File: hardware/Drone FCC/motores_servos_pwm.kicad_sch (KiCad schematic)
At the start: 13 parts, among them J301 ESC 1, J302 ESC 2, J303 ESC 3, J304 ESC 4, J305 ESC 5, J306 ESC 6, J307 ESC 7, J308 ESC 8, J309 SERVO 1, J310 SERVO 2, J311 SERVO 3, J312 SERVO 4, J313 Power Servo

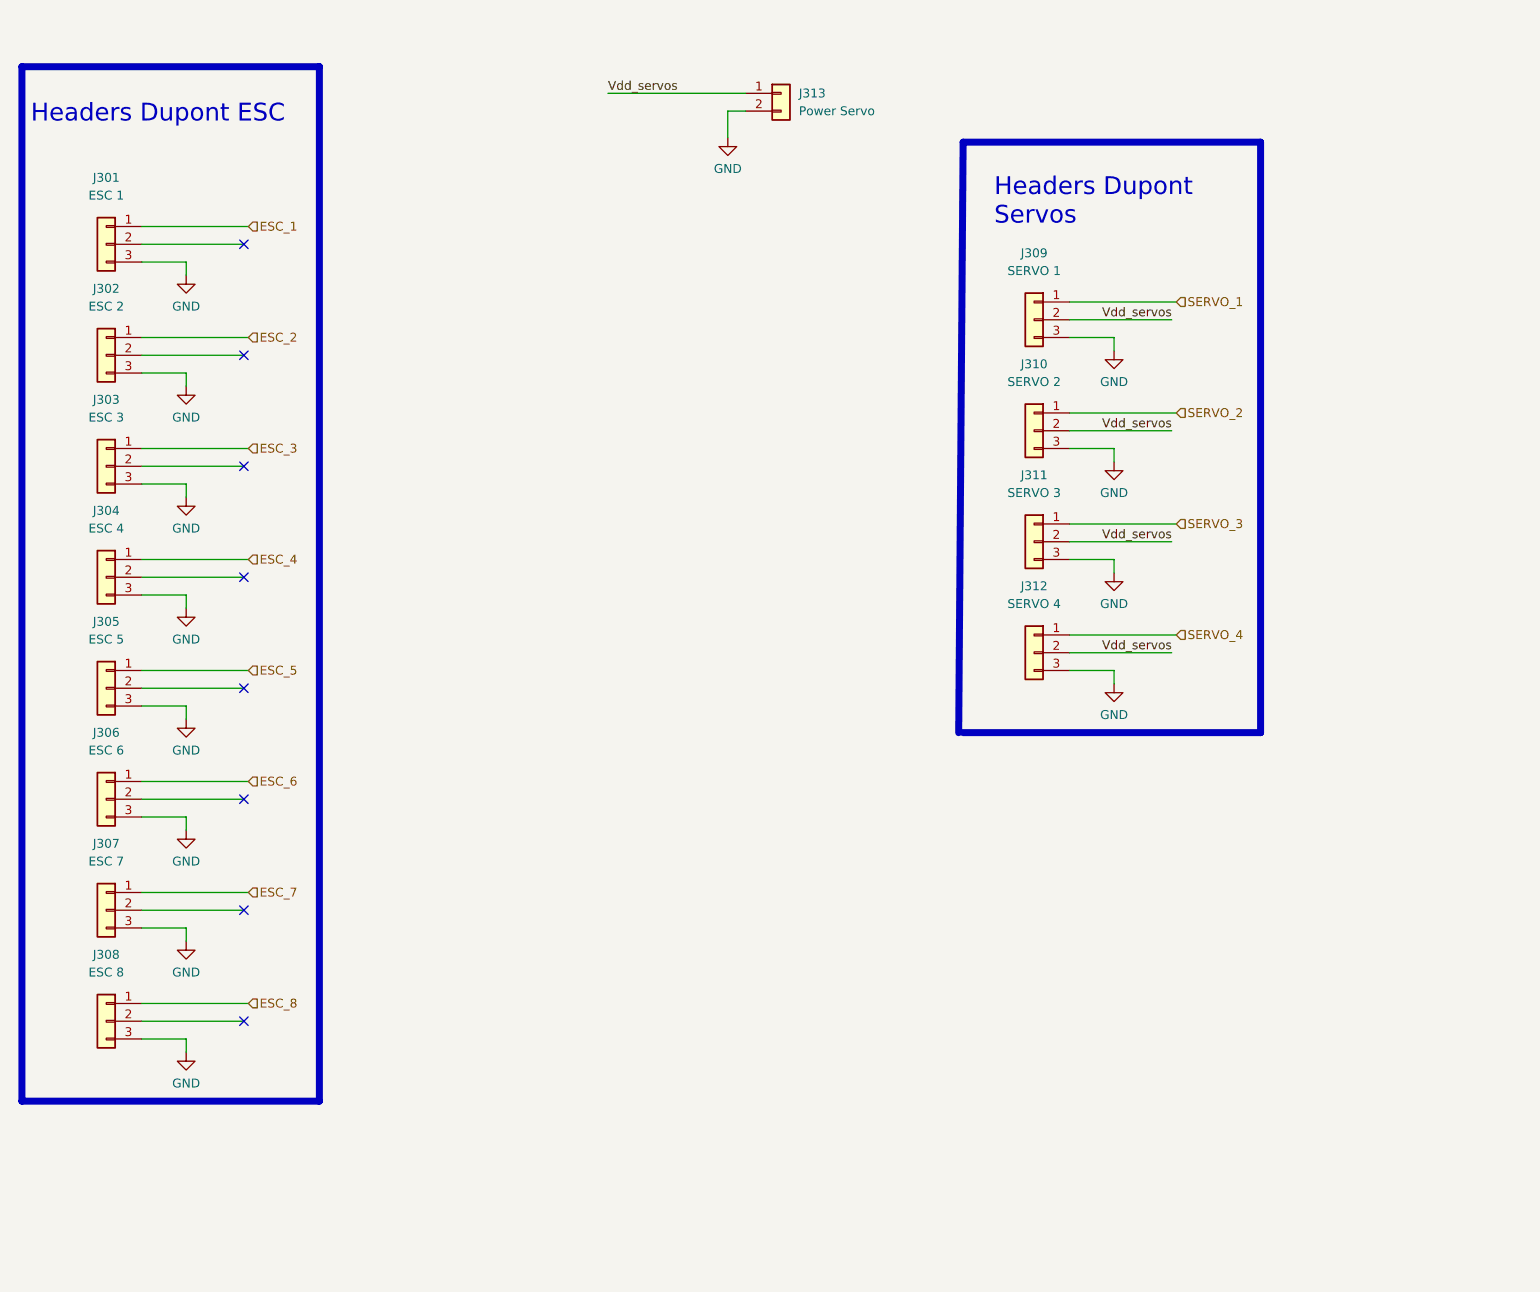
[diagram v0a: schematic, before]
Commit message: added missing TVS diodes
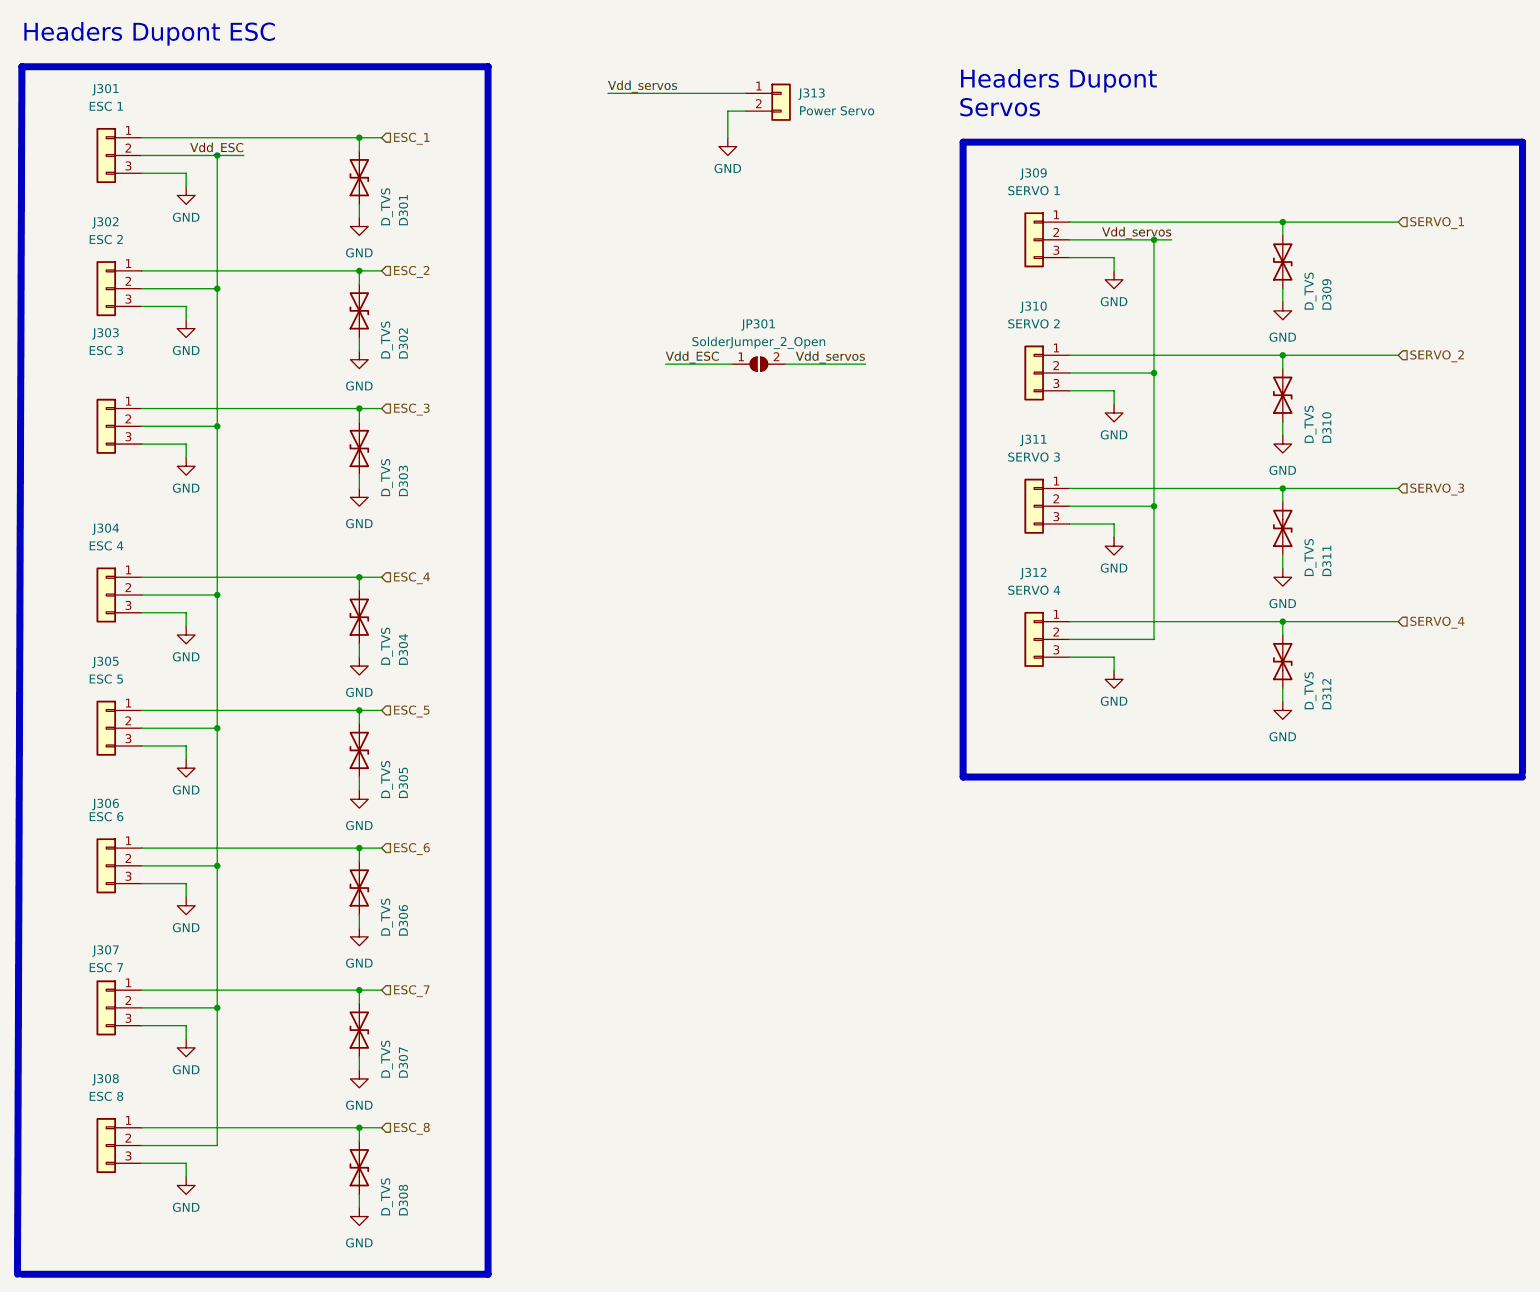
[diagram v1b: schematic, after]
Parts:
- added D301, D302, D303, D304, D305, D306, D307, D308, D309, D310, D311, D312: D_TVS, Diode_SMD:D_0402_1005Metric_Pad0.77x0.64mm_HandSolder, symbol Device:D_TVS
- added JP301: SolderJumper_2_Open, Jumper:SolderJumper-2_P1.3mm_Open_Pad1.0x1.5mm, symbol Jumper:SolderJumper_2_Open
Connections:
- net ESC_1: now also D301.2 (A2)
- net ESC_2: now also D302.2 (A2)
- net ESC_3: now also D303.2 (A2)
- net ESC_4: now also D304.2 (A2)
- net ESC_5: now also D305.2 (A2)
- net ESC_6: now also D306.2 (A2)
- net ESC_7: now also D307.2 (A2)
- net ESC_8: now also D308.2 (A2)
- net GND: now also D301.1 (A1), D302.1 (A1), D303.1 (A1), D304.1 (A1), D305.1 (A1), D306.1 (A1), D307.1 (A1), D308.1 (A1), D309.1 (A1), D310.1 (A1), D311.1 (A1), D312.1 (A1)
- net SERVO_1: now also D309.2 (A2)
- net SERVO_2: now also D310.2 (A2)
- net SERVO_3: now also D311.2 (A2)
- net SERVO_4: now also D312.2 (A2)
- net Vdd_servos: now also JP301.2 (B)
- net Vdd_ESC: now reaches J305.2 (Pin_2)
- net Vdd_ESC: now also J301.2 (Pin_2), J302.2 (Pin_2), J303.2 (Pin_2), J304.2 (Pin_2), J306.2 (Pin_2), J307.2 (Pin_2), J308.2 (Pin_2), JP301.1 (A)
- no-connect marks 8 -> 0
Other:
- moved on the sheet: J301, J302, J303, J304, J305, J306, J307, J308, J309, J310, J311, J312
